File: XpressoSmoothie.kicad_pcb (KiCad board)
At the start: 2 copper layers, 99.7 x 99.7 mm, 130 parts, among them J1 HEADER_4, J10 HEADER_3X2, J11 Pwr_in, J12 HEADER_4, J13 HEADER_4X2, J14 HEADER_3X2, J15 HEADER_4, J16 HEADER_4, J17 HEADER_4, J172 HEADER_2, J18 HEADER_4, J19 HEADER_2, J2 HEADER_4, J20 HEADER_2, J21 HEADER_2, J22 HEADER_2, J23 HEADER_4, J232 HEADER_2, J24 HEADER_4, J25 HEADER_4, J252 HEADER_2, J26 USB, J27 HEADER_4, J28 MICROSD-MOLEX, J3 HEADER_3, J4 HEADER_3X2, J5 HEADER_3X2, J6 LPCXPRESSO_GENERIC_HEADER, J7 HEADER_4, J8 HEADER_4, J9 HEADER_3X2, M1 LOGO_OSHW, M2 LOGO_OSHW, Q1 IRLB 8743, Q2 IRLB 8743, Q3 IRLB 8743, Q4 IRLB 8743, SW1 SW_PUSH, SW2 SW_PUSH, U1 POLOLU_A4988, U10 TC4422A, U11 TC4422A, U12 LM1117-3.3, U2 POLOLU_A4988, U3 POLOLU_A4988, U4 POLOLU_A4988, U5 POLOLU_A4988, U7 LM7809CT, U8 TC4422A, U9 TC4422A

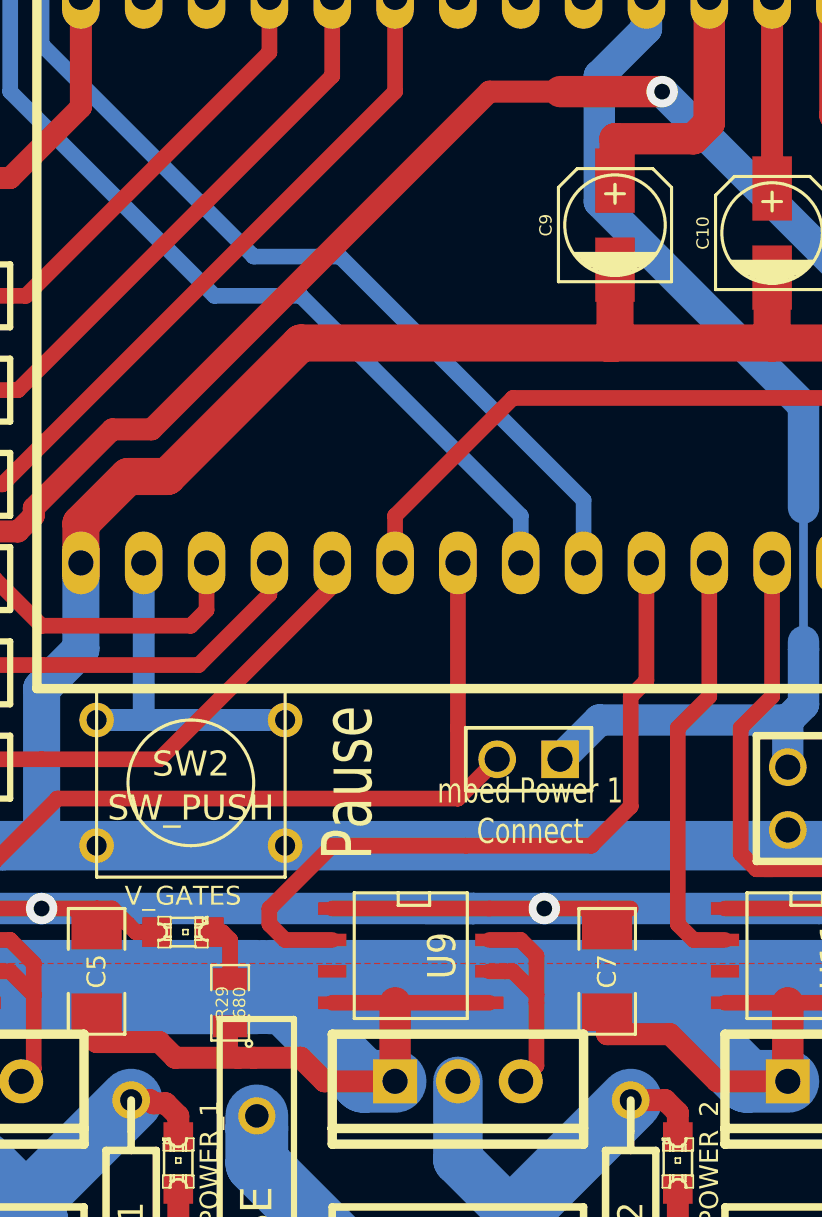
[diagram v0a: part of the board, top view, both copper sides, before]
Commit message: First set of gerbers created. Barring major catastrophe, they will be sent off tomorrow for fabrication.
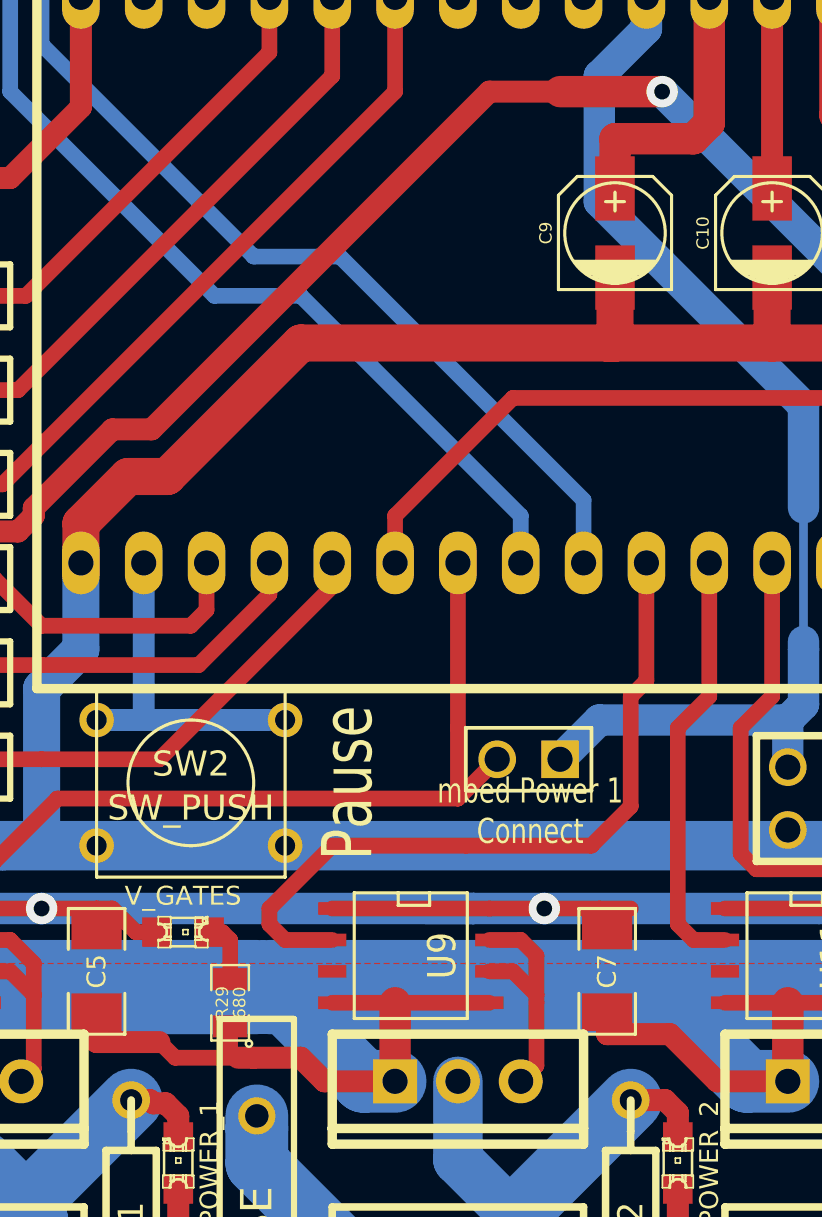
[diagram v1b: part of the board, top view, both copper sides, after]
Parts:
- moved C9 0.32 mm to (118.7, 103.5)
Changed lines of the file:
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@@
     (links 344)
     (no_connects 11)
-    (area 71.742299 53.962299 171.462701 153.682701)
+    (area 56.388 52.51262 179.864657 163.2712)
     (thickness 1.6)
     (drawings 36)
@@
     (18 B.Paste user)
     (19 F.Paste user)
-    (20 B.SilkS user hide)
+    (20 B.SilkS user)
     (21 F.SilkS user)
     (22 B.Mask user)
@@
     (user_trace_width 3.81)
     (trace_clearance 0.2)
-    (zone_clearance 0.635)
+    (zone_clearance 0.508)
     (zone_45_only yes)
     (trace_min 0.35)
@@
     (pad_drill 0.6)
     (pad_to_mask_clearance 0.254)
-    (aux_axis_origin 0 0)
+    (aux_axis_origin 71.755 153.67)
     (visible_elements 7FFFFA3F)
     (pcbplotparams
       (layerselection 15761409)
       (usegerberextensions true)
-      (excludeedgelayer true)
+      (excludeedgelayer false)
       (linewidth 0.150000)
       (plotframeref false)
       (viasonmask false)
       (mode 1)
-      (useauxorigin false)
+      (useauxorigin true)
       (hpglpennumber 1)
       (hpglpenspeed 20)
@@
       (plotothertext true)
       (plotinvisibletext false)
-      (padsonsilk false)
+      (padsonsilk true)
       (subtractmaskfromsilk false)
       (outputformat 1)
@@
   )
   (module c_elec_4x5.3 (layer F.Cu)
-    (at 118.745 103.1875 90)
+    (at 118.745 103.505 90)
     (descr "SMT capacitor, aluminium electrolytic, 4x5.3")
     (fp_text reference C9 (at 0 -2.794 90) (layer F.SilkS)
@@
   (segment (start 103.8225 136.8425) (end 103.505 136.8425) (width 0.635) (layer F.Cu) (net 20))
   (segment (start 97.79 135.001) (end 97.79 136.2075) (width 0.889) (layer F.Cu) (net 20))
-  (segment (start 100.965 136.8425) (end 100.33 136.2075) (width 0.889) (layer F.Cu) (net 20))
+  (segment (start 100.965 136.8425) (end 100.33 136.2075) (width 0.635) (layer F.Cu) (net 20))
   (segment (start 100.33 136.2075) (end 97.79 136.2075) (width 0.889) (layer F.Cu) (net 20))
   (segment (start 106.9975 137.795) (end 109.855 137.795) (width 0.889) (layer F.Cu) (net 20))
@@
   (segment (start 106.9975 137.795) (end 106.045 136.8425) (width 0.889) (layer F.Cu) (net 20))
   (segment (start 104.14 136.8425) (end 103.505 136.8425) (width 0.889) (layer F.Cu) (net 20))
-  (segment (start 103.505 136.8425) (end 100.965 136.8425) (width 0.889) (layer F.Cu) (net 20))
+  (segment (start 103.505 136.8425) (end 100.965 136.8425) (width 0.635) (layer F.Cu) (net 20))
   (segment (start 125.73 137.795) (end 122.8725 137.795) (width 0.889) (layer F.Cu) (net 20))
   (segment (start 118.4275 135.89) (end 118.4275 135.001) (width 0.889) (layer F.Cu) (net 20))

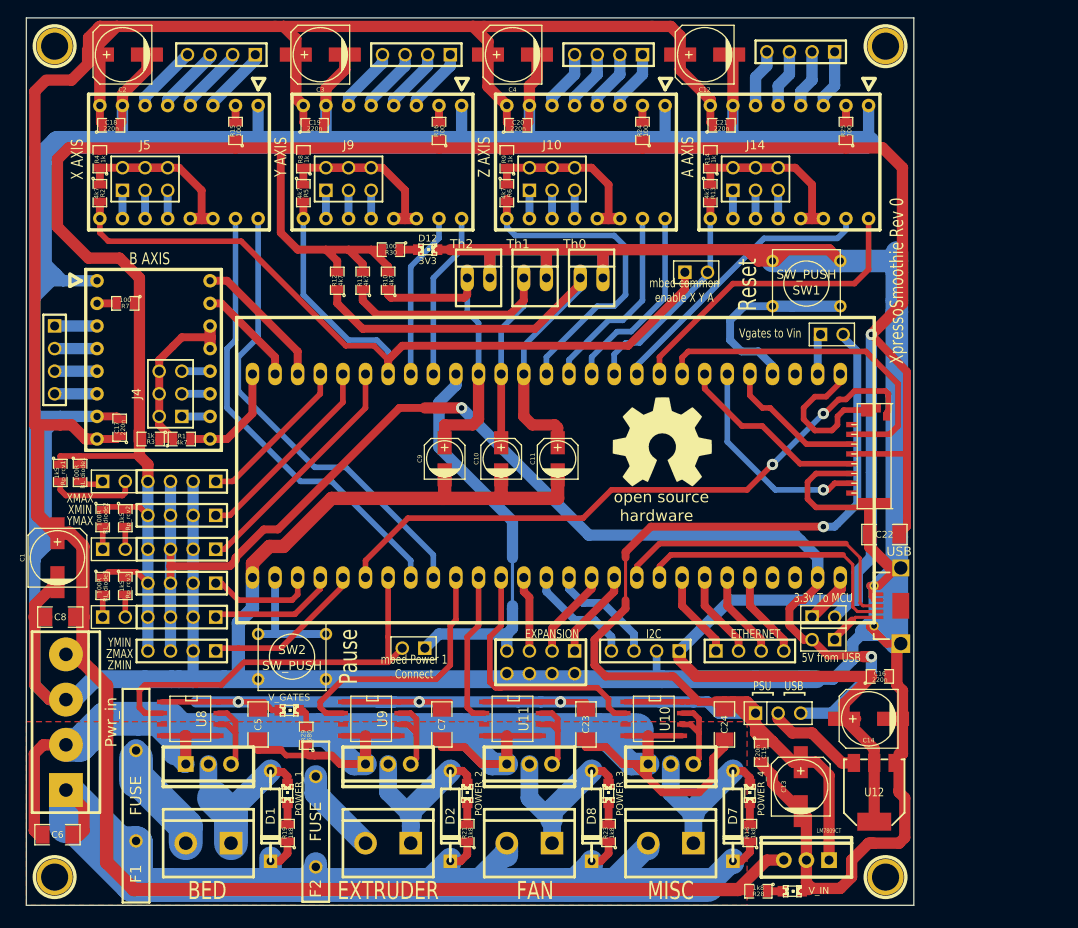
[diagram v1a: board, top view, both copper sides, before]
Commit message: fill zones
added fill
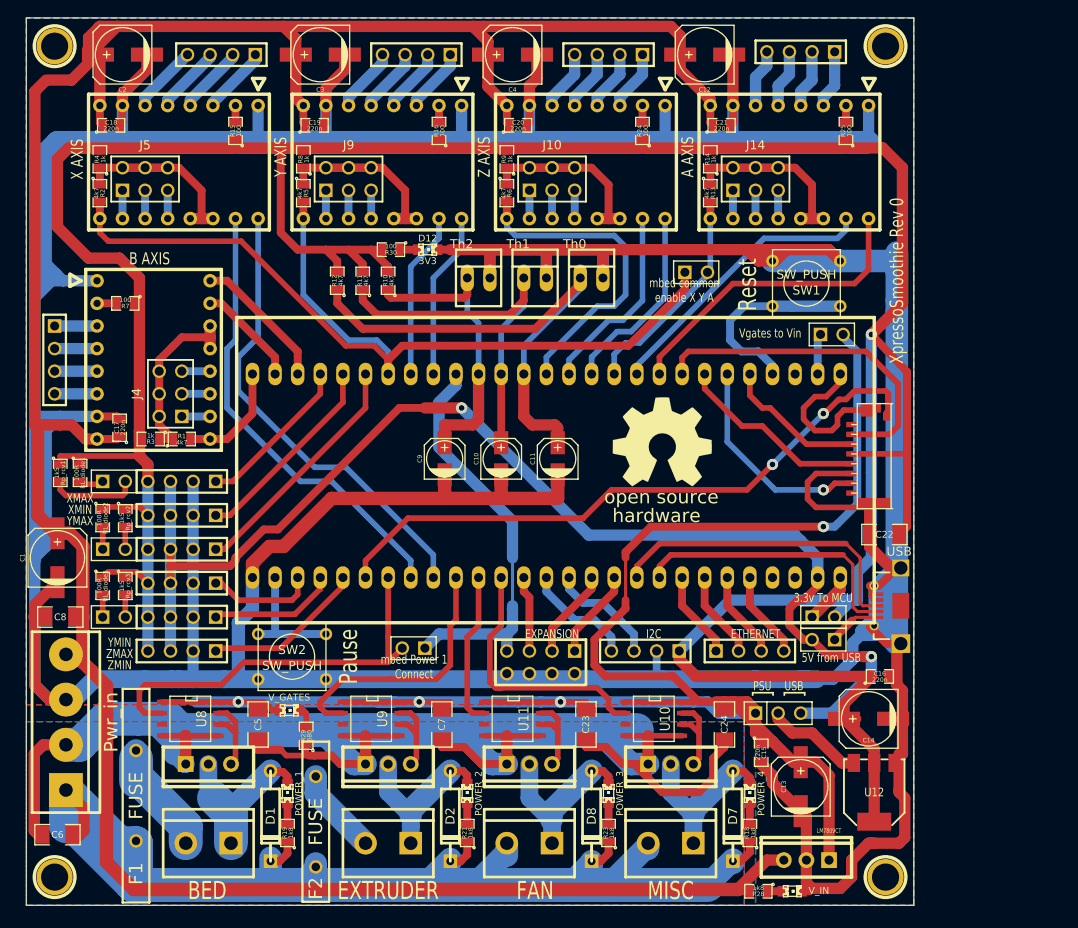
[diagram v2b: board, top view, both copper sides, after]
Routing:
- added copper zone on B.Cu, net (none)
- added copper zone on F.Cu, net (none)
- added copper zone on B.Cu, net GND
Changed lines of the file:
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@@
-(kicad_pcb (version 3) (host pcbnew "(2013-mar-13)-testing")
+(kicad_pcb (version 3) (host pcbnew "(2013-05-16 BZR 4016)-stable")
   (general
     (links 344)
@@
     (user_trace_width 3.81)
     (trace_clearance 0.2)
-    (zone_clearance 0.508)
+    (zone_clearance 0.889)
     (zone_45_only yes)
     (trace_min 0.35)
@@
     (descr "Pololu/Stepstick driver carrier")
     (fp_text reference U2 (at 0 -10.414 180) (layer F.SilkS) hide
-      (effects (font (thickness 0.3048)))
+      (effects (font (size 1.524 1.524) (thickness 0.3048)))
     )
     (fp_text value POLOLU_A4988 (at 0.762 -2.286 180) (layer F.SilkS) hide
-      (effects (font (thickness 0.3048)))
+      (effects (font (size 1.524 1.524) (thickness 0.3048)))
     )
     (fp_line (start -9.652 3.048) (end -8.89 1.778) (layer F.SilkS) (width 0.381))
@@
     (descr "Pololu/Stepstick driver carrier")
     (fp_text reference U4 (at 0 -10.414 180) (layer F.SilkS) hide
-      (effects (font (thickness 0.3048)))
+      (effects (font (size 1.524 1.524) (thickness 0.3048)))
     )
     (fp_text value POLOLU_A4988 (at 0.762 -2.286 180) (layer F.SilkS) hide
-      (effects (font (thickness 0.3048)))
+      (effects (font (size 1.524 1.524) (thickness 0.3048)))
     )
     (fp_line (start -9.652 3.048) (end -8.89 1.778) (layer F.SilkS) (width 0.381))
@@
     (descr "Pololu/Stepstick driver carrier")
     (fp_text reference U5 (at 0 -10.414 180) (layer F.SilkS) hide
-      (effects (font (thickness 0.3048)))
+      (effects (font (size 1.524 1.524) (thickness 0.3048)))
     )
     (fp_text value POLOLU_A4988 (at 0.762 -2.286 180) (layer F.SilkS) hide
-      (effects (font (thickness 0.3048)))
+      (effects (font (size 1.524 1.524) (thickness 0.3048)))
     )
     (fp_line (start -9.652 3.048) (end -8.89 1.778) (layer F.SilkS) (width 0.381))
@@
     (descr "Pololu/Stepstick driver carrier")
     (fp_text reference U1 (at 0 -10.414 270) (layer F.SilkS) hide
-      (effects (font (thickness 0.3048)))
+      (effects (font (size 1.524 1.524) (thickness 0.3048)))
     )
     (fp_text value POLOLU_A4988 (at 0.762 -2.286 270) (layer F.SilkS) hide
-      (effects (font (thickness 0.3048)))
+      (effects (font (size 1.524 1.524) (thickness 0.3048)))
     )
     (fp_line (start -9.652 3.048) (end -8.89 1.778) (layer F.SilkS) (width 0.381))
@@
     (descr "Pololu/Stepstick driver carrier")
     (fp_text reference U3 (at 0 -10.414 180) (layer F.SilkS) hide
-      (effects (font (thickness 0.3048)))
+      (effects (font (size 1.524 1.524) (thickness 0.3048)))
     )
     (fp_text value POLOLU_A4988 (at 0.762 -2.286 180) (layer F.SilkS) hide
-      (effects (font (thickness 0.3048)))
+      (effects (font (size 1.524 1.524) (thickness 0.3048)))
     )
     (fp_line (start -9.652 3.048) (end -8.89 1.778) (layer F.SilkS) (width 0.381))
@@
     (at 104.267 144.272 90)
     (fp_text reference F2 (at -7.493 0 90) (layer F.SilkS)
-      (effects (font (thickness 0.3048)))
+      (effects (font (size 1.524 1.524) (thickness 0.3048)))
     )
     (fp_text value FUSE (at 0 0 90) (layer F.SilkS)
-      (effects (font (thickness 0.3048)))
+      (effects (font (size 1.524 1.524) (thickness 0.3048)))
     )
     (fp_line (start -8.99922 1.50114) (end -8.99922 -1.50114) (layer F.SilkS) (width 0.254))
@@
     (at 84.074 141.351 90)
     (fp_text reference F1 (at -8.763 0 90) (layer F.SilkS)
-      (effects (font (thickness 0.3048)))
+      (effects (font (size 1.524 1.524) (thickness 0.3048)))
     )
     (fp_text value FUSE (at 0 0 90) (layer F.SilkS)
-      (effects (font (thickness 0.3048)))
+      (effects (font (size 1.524 1.524) (thickness 0.3048)))
     )
     (fp_line (start -11.99896 1.50114) (end 11.99896 1.50114) (layer F.SilkS) (width 0.254))
@@
     (at 167.005 87.63 180)
     (fp_text reference J6 (at 5.334 -39.624 180) (layer F.SilkS) hide
-      (effects (font (thickness 0.3048)))
+      (effects (font (size 1.524 1.524) (thickness 0.3048)))
     )
     (fp_text value LPCXPRESSO_GENERIC_HEADER (at 12.954 -36.576 180) (layer F.SilkS) hide
-      (effects (font (thickness 0.3048)))
+      (effects (font (size 1.524 1.524) (thickness 0.3048)))
     )
     (fp_line (start 71.628 0) (end 71.628 -34.29) (layer F.SilkS) (width 0.381))
@@
     )
     (fp_text value Pwr_in (at 0 5.08 90) (layer F.SilkS)
-      (effects (font (thickness 0.3048)))
+      (effects (font (size 1.524 1.524) (thickness 0.3048)))
     )
     (fp_line (start -10.16 -3.81) (end -10.16 3.81) (layer F.SilkS) (width 0.3048))
@@
     (tags DEV)
     (fp_text reference J22 (at 0 -5.08 180) (layer F.SilkS) hide
-      (effects (font (thickness 0.3048)))
+      (effects (font (size 1.524 1.524) (thickness 0.3048)))
     )
     (fp_text value HEADER_2 (at 0 5.08 180) (layer F.SilkS) hide
-      (effects (font (thickness 0.3048)))
+      (effects (font (size 1.524 1.524) (thickness 0.3048)))
     )
     (fp_line (start 5.08 2.54) (end -5.08 2.54) (layer F.SilkS) (width 0.3048))
@@
     (tags DEV)
     (fp_text reference J19 (at 0 -5.08 180) (layer F.SilkS) hide
-      (effects (font (thickness 0.3048)))
+      (effects (font (size 1.524 1.524) (thickness 0.3048)))
     )
     (fp_text value HEADER_2 (at 0 5.08 180) (layer F.SilkS) hide
-      (effects (font (thickness 0.3048)))
+      (effects (font (size 1.524 1.524) (thickness 0.3048)))
     )
     (fp_line (start 5.08 2.54) (end -5.08 2.54) (layer F.SilkS) (width 0.3048))
@@
     (tags DEV)
     (fp_text reference J20 (at 0 -5.08 180) (layer F.SilkS) hide
-      (effects (font (thickness 0.3048)))
+      (effects (font (size 1.524 1.524) (thickness 0.3048)))
     )
     (fp_text value HEADER_2 (at 0 5.08 180) (layer F.SilkS) hide
-      (effects (font (thickness 0.3048)))
+      (effects (font (size 1.524 1.524) (thickness 0.3048)))
     )
     (fp_line (start 5.08 2.54) (end -5.08 2.54) (layer F.SilkS) (width 0.3048))
@@
     (tags DEV)
     (fp_text reference J21 (at 0 -5.08 180) (layer F.SilkS) hide
-      (effects (font (thickness 0.3048)))
+      (effects (font (size 1.524 1.524) (thickness 0.3048)))
     )
     (fp_text value HEADER_2 (at 0 5.08 180) (layer F.SilkS) hide
-      (effects (font (thickness 0.3048)))
+      (effects (font (size 1.524 1.524) (thickness 0.3048)))
     )
     (fp_line (start 5.08 2.54) (end -5.08 2.54) (layer F.SilkS) (width 0.3048))
@@
     )
     (fp_text user hardware (at -0.64516 8.30072) (layer F.SilkS)
-      (effects (font (thickness 0.3048)))
+      (effects (font (size 1.524 1.524) (thickness 0.3048)))
     )
     (fp_text user "open source" (at -0.09906 6.20014) (layer F.SilkS)
-      (effects (font (thickness 0.3048)))
+      (effects (font (size 1.524 1.524) (thickness 0.3048)))
     )
     (fp_poly (pts (xy -3.37312 4.99872) (xy -3.3147 4.96824) (xy -3.18516 4.88696) (xy -2.99974 4.76504)
@@
     (connect_pads yes (clearance 0.635))
     (min_thickness 0.508)
-    (fill (arc_segments 32) (thermal_gap 0.635) (thermal_bridge_width 1.5))
+    (fill (arc_segments 16) (thermal_gap 0.635) (thermal_bridge_width 1.5))
     (polygon
       (pts
-        (xy 71.755 133.0325) (xy 152.7175 133.0325) (xy 152.7175 153.67) (xy 71.755 153.67)
+        (xy 71.755 133.0325) (xy 152.4 133.0325) (xy 152.4 153.67) (xy 71.755 153.67)
+      )
+    )
+  )
+  (zone (net 0) (net_name "") (layer B.Cu) (hatch edge 0.508)
+    (connect_pads (clearance 0.635))
+    (min_thickness 0.508)
+    (keepout (tracks not_allowed) (vias not_allowed) (copperpour not_allowed))
+    (fill (arc_segments 16) (thermal_gap 0.635) (thermal_bridge_width 1.5))
+    (polygon
+      (pts
+        (xy 167.3225 75.2475) (xy 167.3225 77.7875) (xy 171.45 77.7875) (xy 171.45 75.2475)
+      )
+    )
+  )
+  (zone (net 19) (net_name GND) (layer B.Cu) (hatch edge 0.508)
+    (connect_pads (clearance 0.635))
+    (min_thickness 0.635)
+    (fill (arc_segments 16) (thermal_gap 1) (thermal_bridge_width 1.5))
+    (polygon
+      (pts
+        (xy 71.755 131.1275) (xy 153.67 131.1275) (xy 153.67 153.67) (xy 171.45 153.67) (xy 171.45 53.975)
+        (xy 71.755 53.975)
+      )
+    )
+  )
+  (zone (net 0) (net_name "") (layer B.Cu) (hatch edge 0.508)
+    (connect_pads (clearance 0.635))
+    (min_thickness 0.635)
+    (fill (arc_segments 16) (thermal_gap 1) (thermal_bridge_width 1.5))
+    (polygon
+      (pts
+        (xy 71.755 133.0325) (xy 71.755 153.67) (xy 152.4 153.67) (xy 152.4 133.0325)
+      )
+    )
+  )
+  (zone (net 0) (net_name "") (layer F.Cu) (hatch edge 0.508)
+    (connect_pads (clearance 0.889))
+    (min_thickness 0.889)
+    (fill (arc_segments 16) (thermal_gap 1) (thermal_bridge_width 1.5))
+    (polygon
+      (pts
+        (xy 71.755 53.975) (xy 71.755 131.1275) (xy 153.67 131.1275) (xy 153.67 153.67) (xy 171.45 153.67)
+        (xy 171.45 53.975)
       )
     )

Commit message: fillzone
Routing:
- net Vin_rmot: track 317.8 -> 512.5 mm
- net +3.3VP: track 376.3 -> 374.1 mm
